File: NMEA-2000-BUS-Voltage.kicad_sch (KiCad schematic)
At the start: 13 parts, among them J1 Conn_01x03, J3 Conn_01x04_Socket, J4 Conn_01x04, SW1 SW_Push, U1 WeMos_D1_mini, U2 LM7805_TO220

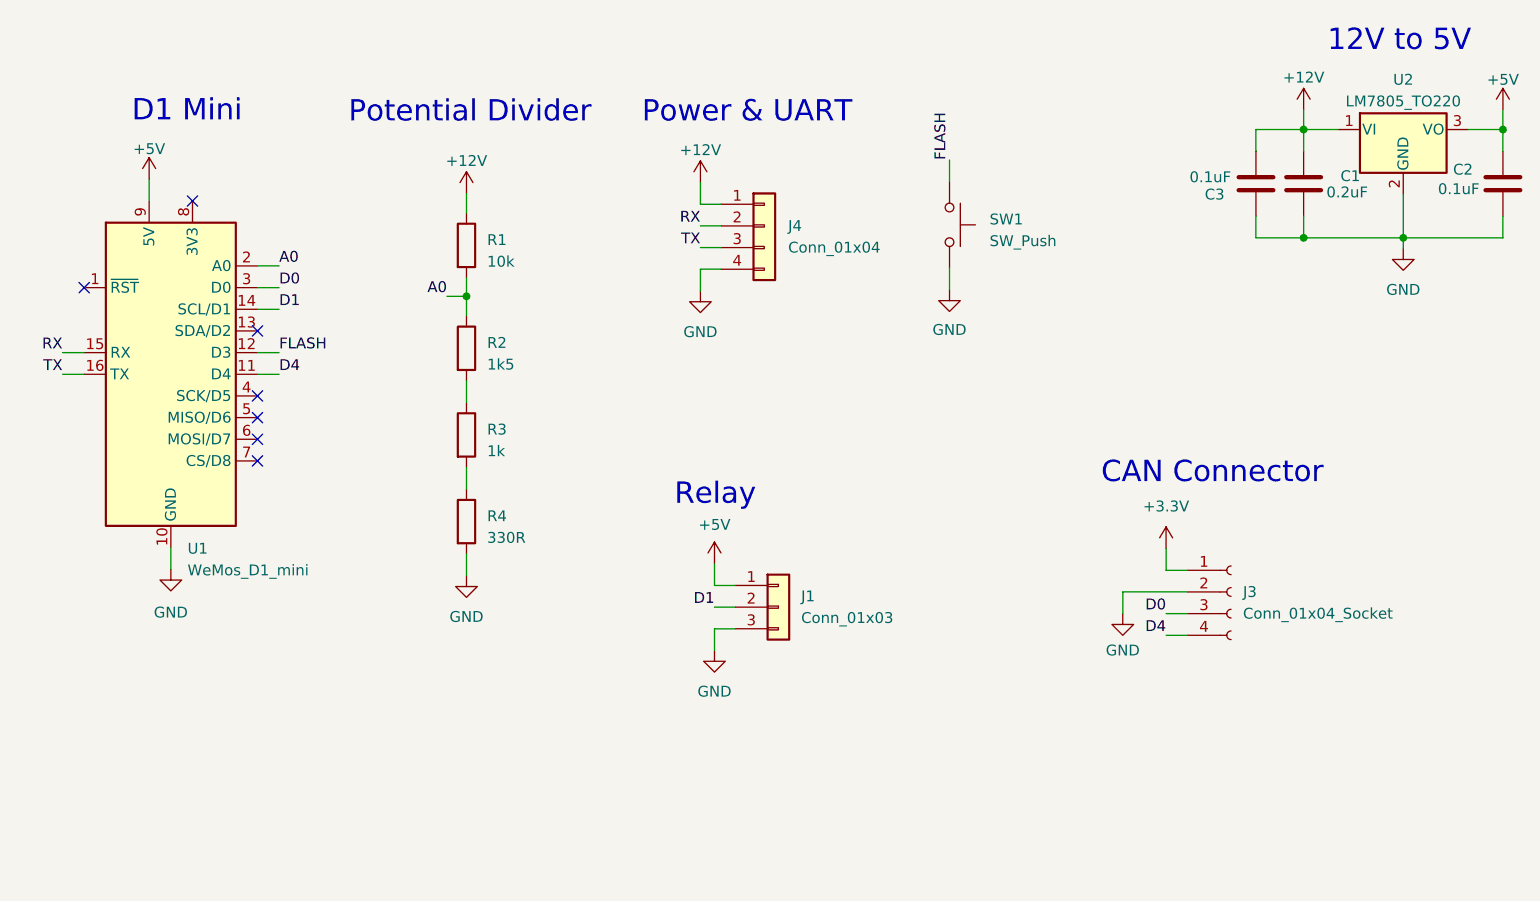
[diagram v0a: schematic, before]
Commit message: Changed D1 Mini to ESP32 Wroom
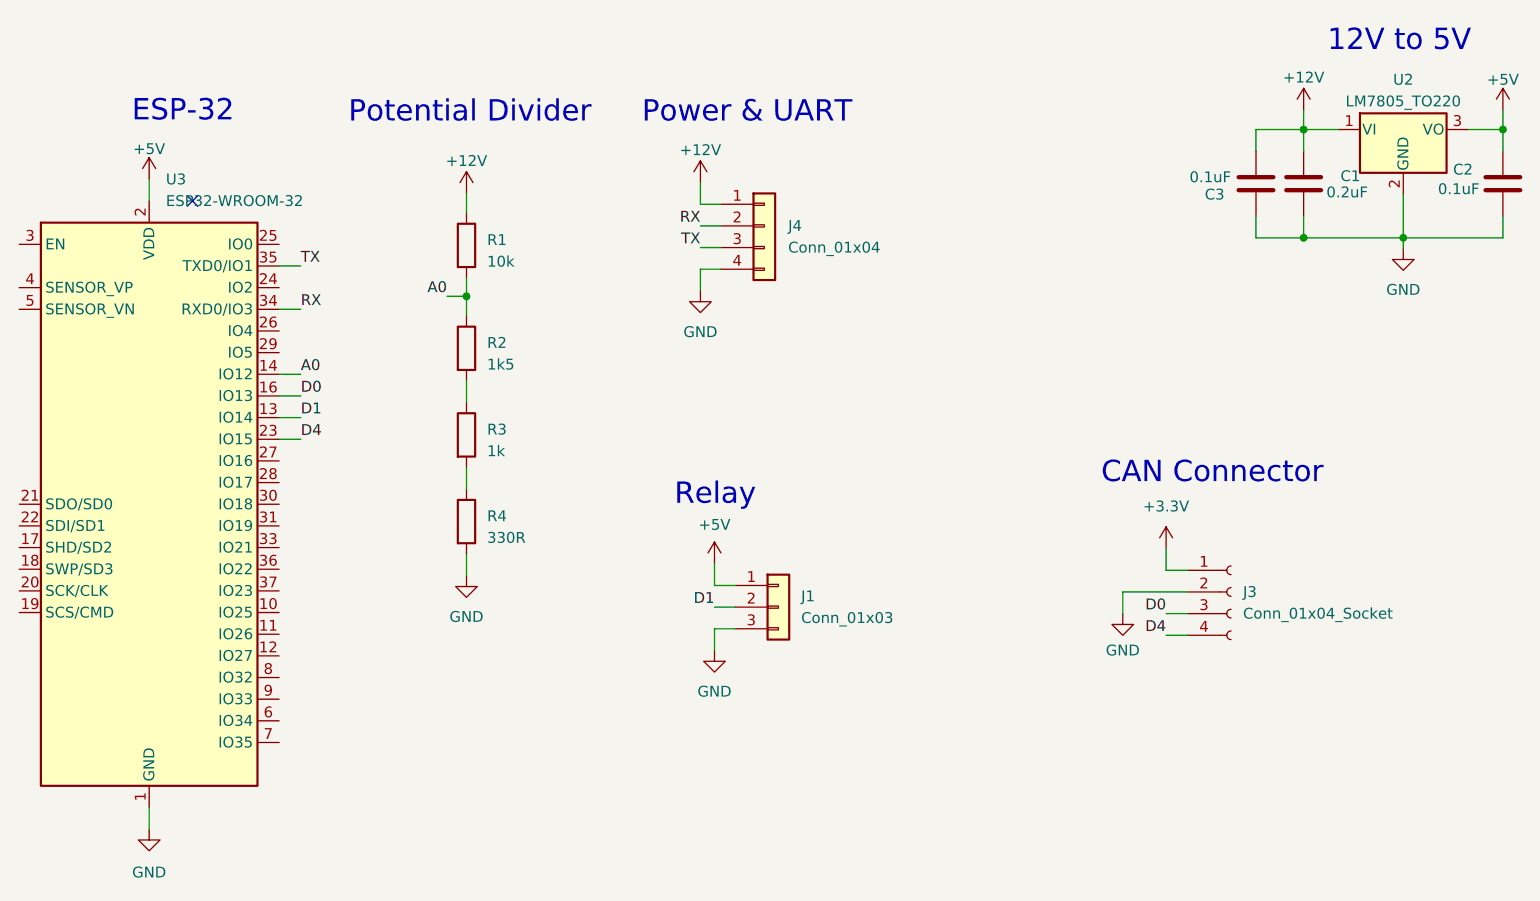
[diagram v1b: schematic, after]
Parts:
- removed SW1: SW_Push, Button_Switch_THT:SW_TH_Tactile_Omron_B3F-10xx, symbol Switch:SW_Push
- removed U1: WeMos_D1_mini, Module:WEMOS_D1_mini_light, symbol MCU_Module:WeMos_D1_mini
- added U3: ESP32-WROOM-32, RF_Module:ESP32-WROOM-32, symbol RF_Module:ESP32-WROOM-32
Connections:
- net +5V: now also U3.2 (VDD)
- net A0: now also U3.14 (IO12)
- net D0: now also U3.16 (IO13)
- net D1: now also U3.13 (IO14)
- net D4: now also U3.23 (IO15)
- net GND: now also U3.1 (GND), U3.15 (GND), U3.38 (GND), U3.39 (GND)
- net RX: now also U3.34 (RXD0/IO3)
- net TX: now also U3.35 (TXD0/IO1)
- no-connect marks 7 -> 1
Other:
- note added: "ESP-32"
- note removed: "D1 Mini"
